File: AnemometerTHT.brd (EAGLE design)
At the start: 150 x 100 mm, 36 parts, among them IC1 TINY2313A, IC2 74HC151D, IC3 74HC151D, IC4 74HC08D, IC5 LM555N, IC6 74HC138D, IC7 74CH14D, IC8 74HC393D, Q1 16MHz

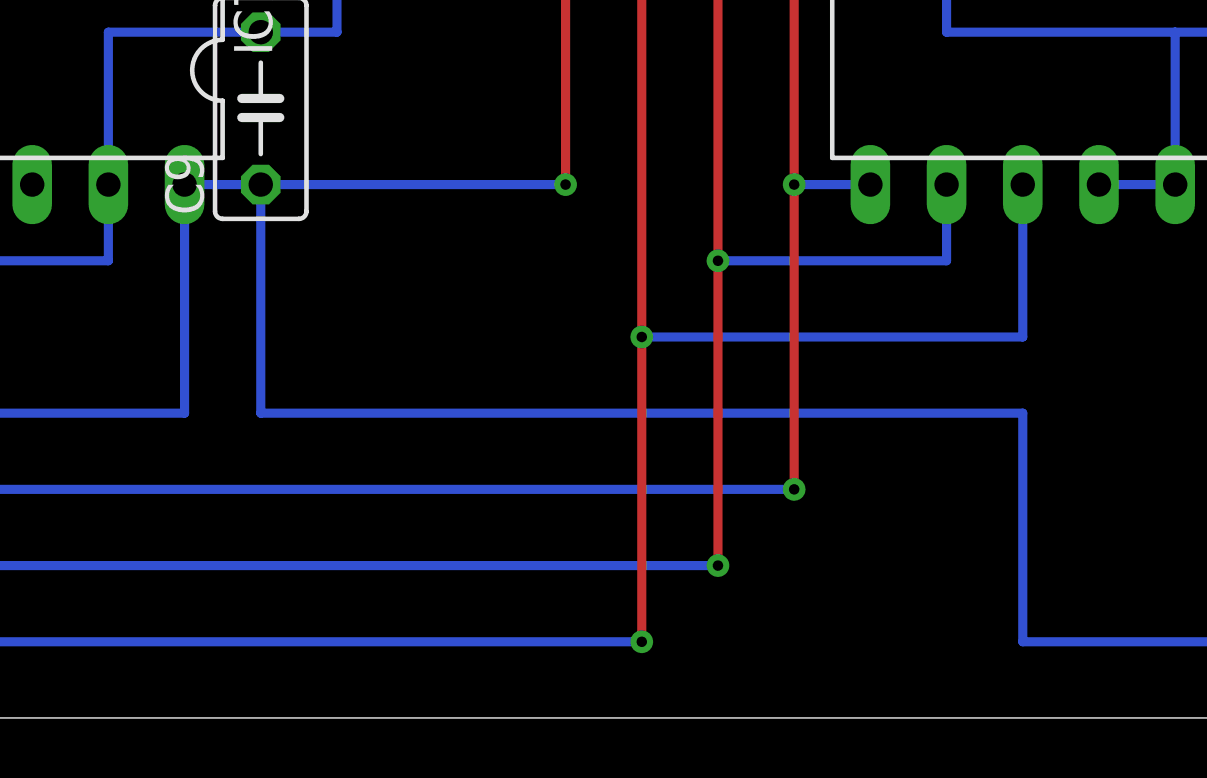
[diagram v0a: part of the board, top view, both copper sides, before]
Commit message: added resistors to make clock run reliable
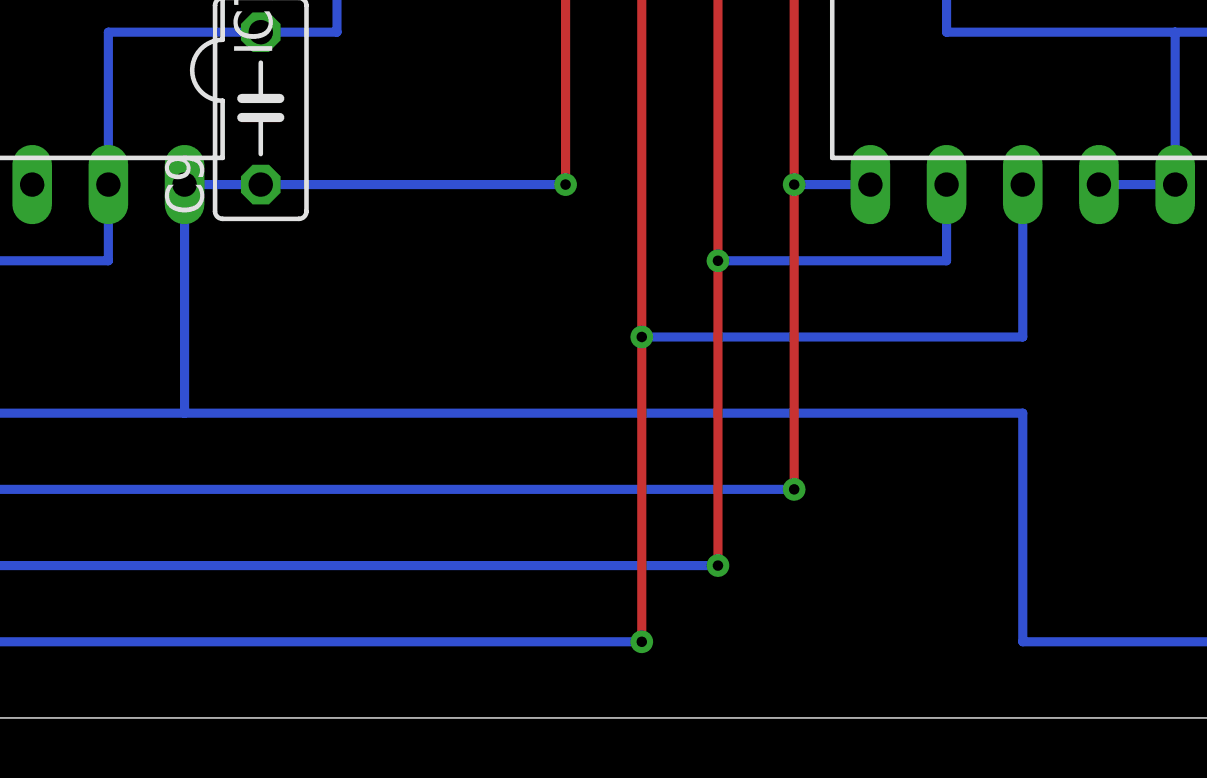
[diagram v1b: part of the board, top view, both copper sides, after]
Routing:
- net VCC: track 569.0 -> 563.9 mm
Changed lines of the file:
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@@
 <attribute name="POPULARITY" value="9" x="59.69" y="-30.48" size="1.778" layer="27" display="off"/>
 <attribute name="SPICEPREFIX" value="C" x="59.69" y="-30.48" size="1.778" layer="27" display="off"/>
-<attribute name="VALUE" x="21.844" y="35.052" size="1.27" layer="27" ratio="10"/>
+<attribute name="VALUE" x="29.464" y="35.052" size="1.27" layer="27" ratio="10"/>
 </element>
 <element name="C4" library="rcl" library_urn="urn:adsk.eagle:library:334" package="C050-030X075" package3d_urn="urn:adsk.eagle:package:23640/1" value="20p" x="60.96" y="35.56" smashed="yes">
@@
 <wire x1="99.06" y1="48.26" x2="101.6" y2="48.26" width="0.3048" layer="16"/>
 <wire x1="99.06" y1="17.78" x2="101.6" y2="17.78" width="0.3048" layer="16"/>
-<wire x1="60.96" y1="17.78" x2="60.96" y2="10.16" width="0.3048" layer="16"/>
 <wire x1="147.32" y1="2.54" x2="147.32" y2="15.24" width="0.3048" layer="16"/>
 <wire x1="86.36" y1="2.54" x2="147.32" y2="2.54" width="0.3048" layer="16"/>
@@
 <via x="66.04" y="83.82" extent="1-16" drill="0.35"/>
 <wire x1="66.04" y1="83.82" x2="66.04" y2="68.58" width="0.3048" layer="1"/>
-<wire x1="60.96" y1="10.16" x2="86.36" y2="10.16" width="0.3048" layer="16"/>
-<wire x1="86.36" y1="10.16" x2="86.36" y2="2.54" width="0.3048" layer="16"/>
+<wire x1="86.36" y1="2.54" x2="86.36" y2="10.16" width="0.3048" layer="16"/>
 <wire x1="71.12" y1="43.18" x2="60.96" y2="43.18" width="0.3048" layer="16"/>
+<wire x1="86.36" y1="10.16" x2="58.42" y2="10.16" width="0.3048" layer="16"/>
 </signal>
 <signal name="PULS">
